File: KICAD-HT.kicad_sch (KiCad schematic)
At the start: 0 parts

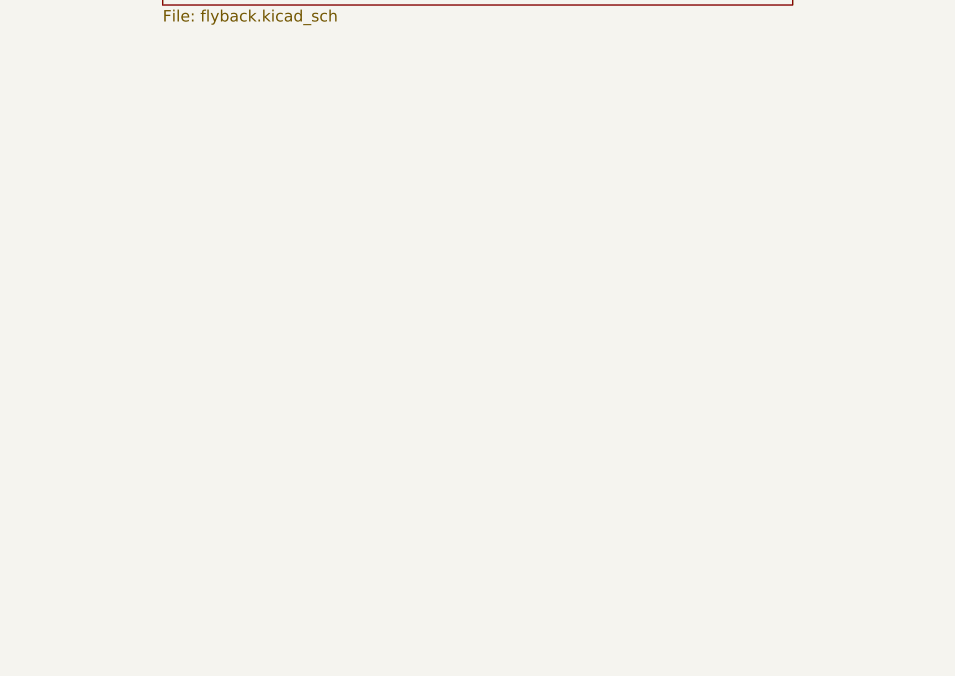
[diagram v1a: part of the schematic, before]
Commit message: Nouvelle feuille limitation-courant.kicad_sch (chaîne rapide + nTRIP isolé)
Générée par script (gen_limitation_courant.py, réutilise les briques de
gen_composants.py -- étiquettes globales uniquement, aucun fil posé),
24 composants : protection d'entrée (R27/C47/D5 BAT54S), TSV791 (×10,09),
référence ATL431 (2,5V + pont diviseur, V_TH≈0,847V -> Ipk_trip≈8,4A),
LMV7219 (comparateur), SN74LVC1G132 (blanking RC+NAND Schmitt),
SN74LVC1G74 (verrou), ISO7710F U19 (retour isolé, sens primaire->contrôle,
inverse de U3).

Sortie isolée nommée directement I_Shunt_ht_comp -- même net déjà posé
sur J2 pin17 (réservé en §18 pour ce signal), aucune modification du
connecteur nécessaire.

Bloc (sheet ...) ajouté à la main dans KICAD-HT.kicad_sch (racine déjà
retouchée à la main pour Polarisation, pas regénérée).

Co-Authored-By: Claude Sonnet 5 <noreply@anthropic.com>
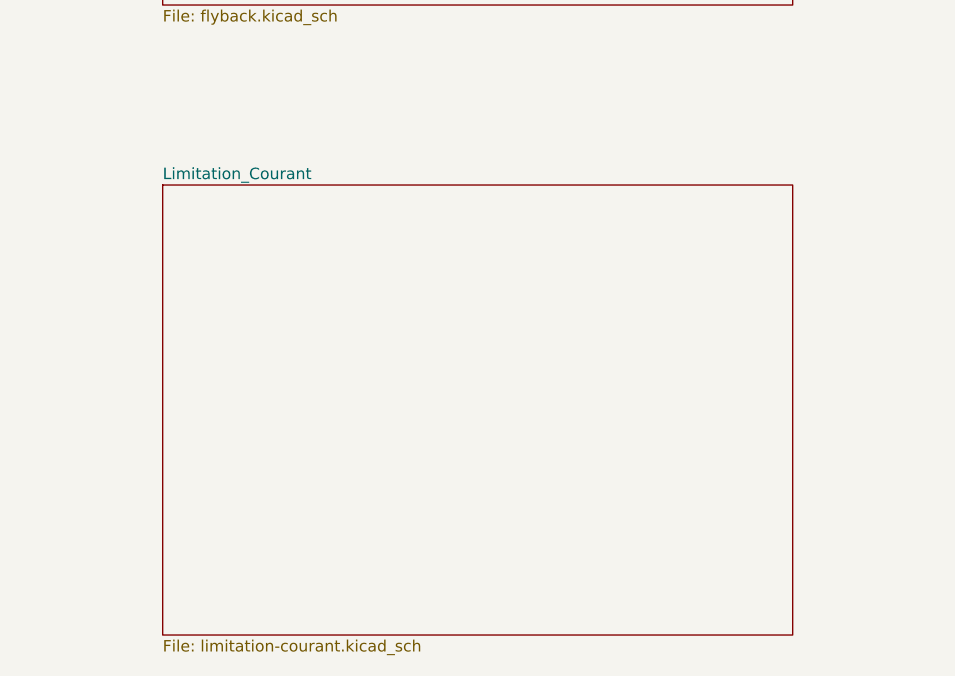
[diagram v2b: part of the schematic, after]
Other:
- added sheet Limitation_Courant (limitation-courant.kicad_sch)
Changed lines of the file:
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@@
+		)
+	)
+	(sheet
+		(at 110 90)
+		(size 70 50)
+		(exclude_from_sim no)
+		(in_bom yes)
+		(on_board yes)
+		(dnp no)
+		(fields_autoplaced yes)
+		(stroke
+			(width 0.1524)
+			(type solid)
+		)
+		(fill
+			(color 0 0 0 0)
+		)
+		(property "Sheetname" "Limitation_Courant"
+			(at 110 89.5 0)
+			(show_name no)
+			(do_not_autoplace no)
+			(effects
+				(font
+					(size 1.27 1.27)
+				)
+				(justify left bottom)
+			)
+		)
+		(property "Sheetfile" "limitation-courant.kicad_sch"
+			(at 110 140.5 0)
+			(show_name no)
+			(do_not_autoplace no)
+			(effects
+				(font
+					(size 1.27 1.27)
+				)
+				(justify left top)
+			)
+		)
+		(instances
+			(project "KICAD-HT"
+				(path "/c8449ac7-87b3-4a93-889f-06dd686c5aff"
+					(page "6")
+				)
+			)
 		)
 	)
